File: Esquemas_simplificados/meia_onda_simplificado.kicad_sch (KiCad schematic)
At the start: 18 parts

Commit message: update cap 4 - rectificadores
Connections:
- net V_{G}+ is gone; now on net V_{G}-: K_{1b}.1 (A)
- net V_{G}-: no longer K_{1a}.1 (A)
- new net V_{G+}: K_{1a}.1 (A)
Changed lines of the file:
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@@
 		(end 111.76 41.91)
 		(stroke
-			(width 0)
-			(type default)
+			(width 0.3)
+			(type dash)
+			(color 255 0 0 1)
 		)
 		(fill
@@
 		(end 74.93 59.69)
 		(stroke
-			(width 0)
-			(type default)
+			(width 0.3)
+			(type dash)
+			(color 0 0 132 1)
 		)
 		(fill
@@
 		)
 	)
-	(label "V_{G}-"
+	(label "V_{G+}"
 		(at 58.42 45.72 180)
 		(fields_autoplaced yes)
@@
 		)
 	)
-	(label "V_{G}+"
+	(label "V_{G}-"
 		(at 58.42 48.26 180)
 		(fields_autoplaced yes)
@@
 		(dnp no)
 		(property "Reference" "K_{7a}"
-			(at 122.936 34.544 0)
+			(at 124.46 36.068 0)
 			(effects
 				(font
@@
 		(dnp no)
 		(property "Reference" "K_{1a}"
-			(at 68.58 35.306 0)
+			(at 68.072 36.576 0)
 			(effects
 				(font
@@
 		)
 		(instances
-			(project ""
+			(project "meia_onda_simplificado"
 				(path "/503ffb7c-03f1-4b74-8c9a-f81a98559f55"
 					(reference "K_{1a}")
@@
 		)
 		(instances
-			(project ""
+			(project "meia_onda_simplificado"
 				(path "/503ffb7c-03f1-4b74-8c9a-f81a98559f55"
 					(reference "R2")
@@
 		(dnp no)
 		(property "Reference" "K_{1b}"
-			(at 69.342 50.8 0)
+			(at 67.818 51.816 0)
 			(effects
 				(font
@@
 		)
 		(instances
-			(project ""
+			(project "meia_onda_simplificado"
 				(path "/503ffb7c-03f1-4b74-8c9a-f81a98559f55"
 					(reference "K_{1b}")
@@
 		(dnp no)
 		(property "Reference" "K_{7b}"
-			(at 122.936 59.944 0)
+			(at 124.968 61.468 0)
 			(effects
 				(font
@@
 		(dnp no)
 		(property "Reference" "K_{6a}"
-			(at 114.046 34.544 0)
+			(at 115.57 36.068 0)
 			(effects
 				(font
@@
 		(dnp no)
 		(property "Reference" "K_{3a}"
-			(at 82.55 35.306 0)
+			(at 81.534 36.576 0)
 			(effects
 				(font
@@
 		)
 		(instances
-			(project ""
+			(project "meia_onda_simplificado"
 				(path "/503ffb7c-03f1-4b74-8c9a-f81a98559f55"
 					(reference "K_{3a}")
@@
 		(dnp no)
 		(property "Reference" "K_{9b}"
-			(at 140.716 59.944 0)
+			(at 142.494 61.468 0)
 			(effects
 				(font
@@
 		(dnp no)
 		(property "Reference" "K_{6b}"
-			(at 114.046 59.944 0)
+			(at 116.078 61.468 0)
 			(effects
 				(font
@@
 		)
 		(instances
-			(project ""
+			(project "meia_onda_simplificado"
 				(path "/503ffb7c-03f1-4b74-8c9a-f81a98559f55"
 					(reference "D1")
@@
 		(dnp no)
 		(property "Reference" "K_{3b}"
-			(at 105.156 35.306 0)
+			(at 104.14 36.83 0)
 			(effects
 				(font
@@
 		)
 		(instances
-			(project ""
+			(project "meia_onda_simplificado"
 				(path "/503ffb7c-03f1-4b74-8c9a-f81a98559f55"
 					(reference "K_{3b}")
@@
 		)
 		(instances
-			(project ""
+			(project "meia_onda_simplificado"
 				(path "/503ffb7c-03f1-4b74-8c9a-f81a98559f55"
 					(reference "R1")
@@
 		)
 		(instances
-			(project ""
+			(project "meia_onda_simplificado"
 				(path "/503ffb7c-03f1-4b74-8c9a-f81a98559f55"
 					(reference "C2")
@@
 		(dnp no)
 		(property "Reference" "K_{8a}"
-			(at 131.826 34.544 0)
+			(at 133.35 36.068 0)
 			(effects
 				(font
@@
 		(dnp no)
 		(property "Reference" "K_{9a}"
-			(at 140.716 34.544 0)
+			(at 142.748 36.068 0)
 			(effects
 				(font
@@
 		)
 		(instances
-			(project ""
+			(project "meia_onda_simplificado"
 				(path "/503ffb7c-03f1-4b74-8c9a-f81a98559f55"
 					(reference "C1")
@@
 		(dnp no)
 		(property "Reference" "K_{4}"
-			(at 93.98 51.308 0)
+			(at 92.964 52.324 0)
 			(effects
 				(font
@@
 		)
 		(instances
-			(project ""
+			(project "meia_onda_simplificado"
 				(path "/503ffb7c-03f1-4b74-8c9a-f81a98559f55"
 					(reference "K_{4}")
@@
 		(dnp no)
 		(property "Reference" "K_{8b}"
-			(at 131.826 59.944 0)
-			(effects
-				(font
+			(at 133.604 61.468 0)
+			(effects
+				(font

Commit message: update rectificação cap 4
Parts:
- added D2: B250C2300-1500A, Diode_THT:Diode_Bridge_19.0x3.5x10.0mm_P5.0mm, symbol Diode_Bridge:B250C2300-1500A
- added K_{2a}, K_{2b}, K_{5a}, K_{5b}: SW_SPST, symbol Switch:SW_SPST
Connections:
- net A: now reaches K_{3b}.2 (B), K_{6a}.2 (B), K_{7a}.2 (B), K_{8a}.2 (B), K_{9a}.2 (B)
- net A: now also K_{5a}.2 (B)
- net B: now reaches K_{4}.2 (B), K_{6b}.1 (A), K_{7b}.1 (A), K_{8b}.1 (A), K_{9b}.1 (A)
- net B: now also K_{5b}.2 (B)
- net V_{G}- renamed V_{G-}
- new net: D2.4 (+), K_{5a}.1 (A)
- new net: D2.2, K_{2a}.2 (B)
- new net: D2.3, K_{2b}.2 (B)
- new net: D2.1 (-), K_{5b}.1 (A)
- new net transf+: K_{2a}.1 (A)
- new net transf-: K_{2b}.1 (A)
- no-connect marks 0 -> 4
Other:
- note added: "Filtragem (Comum)"
- note added: "Meia Onda"
- note added: "Onda Completa"
- moved on the sheet: C1, C2, D1, K_{1a}, K_{1b}, K_{3a}, K_{3b}, K_{4}, K_{6a}, K_{6b}, K_{7a}, K_{7b}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

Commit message: update chap 4 - filtros
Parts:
- added C3: 10uF, Capacitor_THT:CP_Radial_D5.0mm_P2.00mm, symbol Device:C_Polarized
- added K_{10}, K_{11}: SW_SPST, symbol Switch:SW_SPST
- added R3: 1K, Resistor_THT:R_Axial_DIN0207_L6.3mm_D2.5mm_P15.24mm_Horizontal, symbol Device:R
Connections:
- net A: now also C3.2, R3.1
- net V_{G+} renamed v_{g+}
- net v_{g+}: now also K_{10}.1 (A), K_{11}.1 (A)
- net V_{G-} renamed v_{g-}
- new net: K_{10}.2 (B), R3.2
- new net: C3.1, K_{11}.2 (B)
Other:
- note removed: "Filtragem (Comum)"
- note removed: "Meia Onda"
- moved on the sheet: C1, C2, D1, D2, K_{1a}, K_{1b}, K_{2a}, K_{2b}, K_{3a}, K_{3b}, K_{4}, K_{5a}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

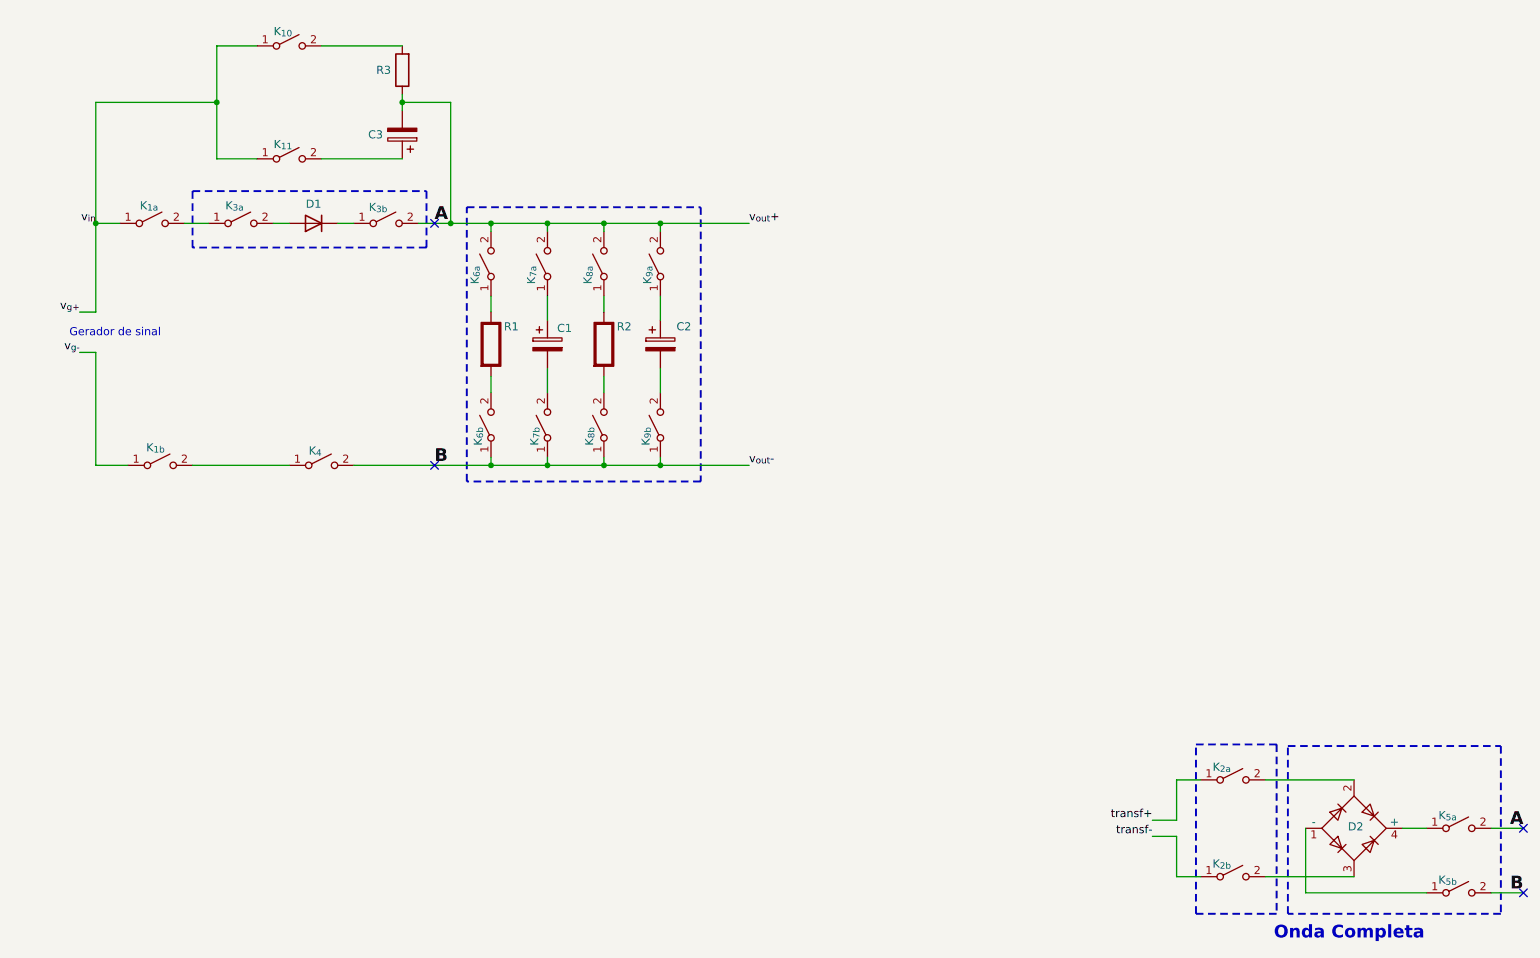
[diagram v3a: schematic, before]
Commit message: update chap 4 - modificação do texto dos filtros e rectificadores
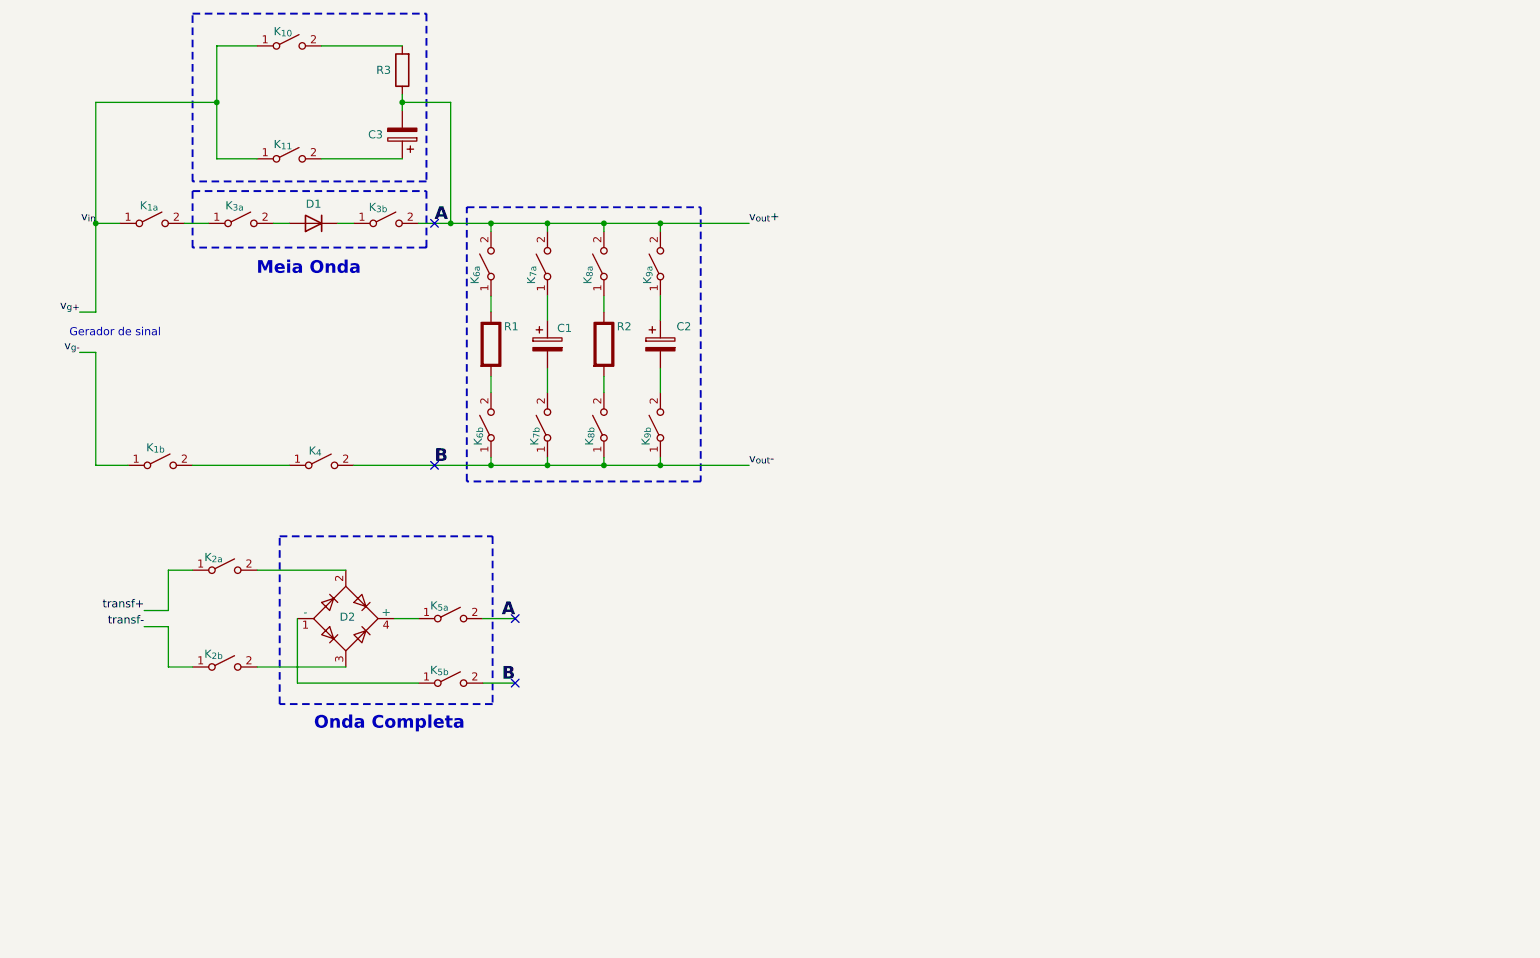
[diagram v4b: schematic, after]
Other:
- note added: "Meia Onda"
- moved on the sheet: D2, K_{2a}, K_{2b}, K_{5a}, K_{5b}
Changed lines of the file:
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@@
 	)
 	(no_connect
-		(at 251.46 142.24)
+		(at 92.71 109.22)
 	)
 	(no_connect
@@
 	)
 	(no_connect
-		(at 251.46 152.4)
+		(at 92.71 119.38)
 	)
 	(wire
@@
 	(wire
 		(pts
-			(xy 210.82 134.62) (xy 224.79 134.62)
-		)
-		(stroke
-			(width 0)
-			(type default)
-		)
-	)
-	(wire
-		(pts
-			(xy 236.22 142.24) (xy 232.41 142.24)
-		)
-		(stroke
-			(width 0)
-			(type default)
-		)
-	)
-	(wire
-		(pts
-			(xy 196.85 143.51) (xy 196.85 149.86)
+			(xy 52.07 101.6) (xy 66.04 101.6)
+		)
+		(stroke
+			(width 0)
+			(type default)
+		)
+	)
+	(wire
+		(pts
+			(xy 77.47 109.22) (xy 73.66 109.22)
+		)
+		(stroke
+			(width 0)
+			(type default)
+		)
+	)
+	(wire
+		(pts
+			(xy 38.1 110.49) (xy 38.1 116.84)
 		)
 		(stroke
@@
 	(wire
 		(pts
-			(xy 196.85 134.62) (xy 196.85 140.97)
+			(xy 38.1 101.6) (xy 38.1 107.95)
 		)
 		(stroke
@@
 	(wire
 		(pts
-			(xy 210.82 149.86) (xy 224.79 149.86)
+			(xy 52.07 116.84) (xy 66.04 116.84)
 		)
 		(stroke
@@
 	(wire
 		(pts
-			(xy 217.17 142.24) (xy 217.17 152.4)
+			(xy 58.42 109.22) (xy 58.42 119.38)
 		)
 		(stroke
@@
 	(wire
 		(pts
-			(xy 196.85 149.86) (xy 200.66 149.86)
+			(xy 38.1 116.84) (xy 41.91 116.84)
 		)
 		(stroke
@@
 	(wire
 		(pts
-			(xy 246.38 142.24) (xy 251.46 142.24)
+			(xy 87.63 109.22) (xy 92.71 109.22)
 		)
 		(stroke
@@
 	(wire
 		(pts
-			(xy 217.17 152.4) (xy 236.22 152.4)
+			(xy 58.42 119.38) (xy 77.47 119.38)
 		)
 		(stroke
@@
 	(wire
 		(pts
-			(xy 193.04 143.51) (xy 196.85 143.51)
+			(xy 34.29 110.49) (xy 38.1 110.49)
 		)
 		(stroke
@@
 	(wire
 		(pts
-			(xy 196.85 134.62) (xy 200.66 134.62)
-		)
-		(stroke
-			(width 0)
-			(type default)
-		)
-	)
-	(wire
-		(pts
-			(xy 246.38 152.4) (xy 251.46 152.4)
+			(xy 38.1 101.6) (xy 41.91 101.6)
+		)
+		(stroke
+			(width 0)
+			(type default)
+		)
+	)
+	(wire
+		(pts
+			(xy 87.63 119.38) (xy 92.71 119.38)
 		)
 		(stroke
@@
 	(wire
 		(pts
-			(xy 193.04 140.97) (xy 196.85 140.97)
+			(xy 34.29 107.95) (xy 38.1 107.95)
 		)
 		(stroke
@@
 	)
 	(rectangle
-		(start 199.898 129.032)
-		(end 212.598 155.702)
+		(start 55.626 96.266)
+		(end 89.154 122.682)
 		(stroke
 			(width 0.3)
 			(type dash)
-			(color 78 222 255 1)
+			(color 0 132 0 1)
 		)
 		(fill
@@
 	)
 	(rectangle
-		(start 214.376 129.286)
-		(end 247.904 155.702)
+		(start 41.91 13.97)
+		(end 78.74 40.386)
 		(stroke
 			(width 0.3)
 			(type dash)
-			(color 255 115 114 1)
+			(color 255 0 255 1)
 		)
 		(fill
@@
 	(text "Onda Completa"
 		(exclude_from_sim no)
-		(at 224.028 158.75 0)
+		(at 72.898 125.73 0)
 		(effects
 			(font
@@
 		)
 	)
+	(text "Meia Onda"
+		(exclude_from_sim no)
+		(at 60.198 54.102 0)
+		(effects
+			(font
+				(size 2 2)
+				(bold yes)
+			)
+		)
+	)
 	(label "B"
-		(at 251.46 152.4 180)
+		(at 92.71 119.38 180)
 		(fields_autoplaced yes)
 		(effects
@@
 	)
 	(label "transf-"
-		(at 193.04 143.51 180)
+		(at 34.29 110.49 180)
 		(fields_autoplaced yes)
 		(effects
@@
 	)
 	(label "transf+"
-		(at 193.04 140.97 180)
+		(at 34.29 107.95 180)
 		(fields_autoplaced yes)
 		(effects
@@
 	)
 	(label "A"
-		(at 251.46 142.24 180)
+		(at 92.71 109.22 180)
 		(fields_autoplaced yes)
 		(effects
@@
 	(symbol
 		(lib_id "Switch:SW_SPST")
-		(at 241.3 142.24 0)
+		(at 82.55 109.22 0)
 		(unit 1)
 		(exclude_from_sim no)
@@
 		(dnp no)
 		(property "Reference" "K_{5a}"
-			(at 239.522 140.208 0)
+			(at 80.772 107.188 0)
 			(effects
 				(font
@@
 		)
 		(property "Value" "SW_SPST"
-			(at 241.3 138.43 0)
+			(at 82.55 105.41 0)
 			(effects
 				(font
@@
 		)
 		(property "Footprint" ""
-			(at 241.3 142.24 0)
+			(at 82.55 109.22 0)
 			(effects
 				(font
@@
 		)
 		(property "Datasheet" "~"
-			(at 241.3 142.24 0)
+			(at 82.55 109.22 0)
 			(effects
 				(font
@@
 		)
 		(property "Description" "Single Pole Single Throw (SPST) switch"
-			(at 241.3 142.24 0)
+			(at 82.55 109.22 0)
 			(effects
 				(font
@@
 	(symbol
 		(lib_id "Switch:SW_SPST")
-		(at 205.74 134.62 0)
+		(at 46.99 101.6 0)
 		(unit 1)
 		(exclude_from_sim no)
@@
 		(dnp no)
 		(property "Reference" "K_{2a}"
-			(at 203.962 132.588 0)
+			(at 45.212 99.568 0)
 			(effects
 				(font
@@
 		)
 		(property "Value" "SW_SPST"
-			(at 205.74 130.81 0)
+			(at 46.99 97.79 0)
 			(effects
 				(font
@@
 		)
 		(property "Footprint" ""
-			(at 205.74 134.62 0)
+			(at 46.99 101.6 0)
 			(effects
 				(font
@@
 		)
 		(property "Datasheet" "~"
-			(at 205.74 134.62 0)
+			(at 46.99 101.6 0)
 			(effects
 				(font
@@
 		)
 		(property "Description" "Single Pole Single Throw (SPST) switch"
-			(at 205.74 134.62 0)
+			(at 46.99 101.6 0)
 			(effects
 				(font
@@
 	(symbol
 		(lib_id "Switch:SW_SPST")
-		(at 205.74 149.86 0)
+		(at 46.99 116.84 0)
 		(unit 1)
 		(exclude_from_sim no)
@@
 		(dnp no)
 		(property "Reference" "K_{2b}"
-			(at 203.962 147.828 0)
+			(at 45.212 114.808 0)
 			(effects
 				(font
@@
 		)
 		(property "Value" "SW_SPST"
-			(at 205.74 146.05 0)
+			(at 46.99 113.03 0)
 			(effects
 				(font
@@
 		)
 		(property "Footprint" ""
-			(at 205.74 149.86 0)
+			(at 46.99 116.84 0)
 			(effects
 				(font
@@
 		)
 		(property "Datasheet" "~"
-			(at 205.74 149.86 0)
+			(at 46.99 116.84 0)
 			(effects
 				(font
@@
 		)
 		(property "Description" "Single Pole Single Throw (SPST) switch"
-			(at 205.74 149.86 0)
+			(at 46.99 116.84 0)
 			(effects
 				(font
@@
 	(symbol
 		(lib_id "Switch:SW_SPST")
-		(at 241.3 152.4 0)
+		(at 82.55 119.38 0)
 		(unit 1)
 		(exclude_from_sim no)
@@
 		(dnp no)
 		(property "Reference" "K_{5b}"
-			(at 239.522 150.368 0)
+			(at 80.772 117.348 0)
 			(effects
 				(font
@@
 		)
 		(property "Value" "SW_SPST"
-			(at 241.3 148.59 0)
+			(at 82.55 115.57 0)
 			(effects
 				(font
@@
 		)
 		(property "Footprint" ""
-			(at 241.3 152.4 0)
+			(at 82.55 119.38 0)
 			(effects
 				(font
@@
 		)
 		(property "Datasheet" "~"
-			(at 241.3 152.4 0)
+			(at 82.55 119.38 0)
 			(effects
 				(font
@@
 		)
 		(property "Description" "Single Pole Single Throw (SPST) switch"
-			(at 241.3 152.4 0)
+			(at 82.55 119.38 0)
 			(effects
 				(font
@@
 	(symbol
 		(lib_id "Diode_Bridge:B250C2300-1500A")
-		(at 224.79 142.24 0)
+		(at 66.04 109.22 0)
 		(unit 1)
 		(exclude_from_sim no)
@@
 		(dnp no)
 		(property "Reference" "D2"
-			(at 225.044 141.986 0)
+			(at 66.294 108.966 0)
 			(effects
 				(font
@@
 		)
 		(property "Value" "B250C2300-1500A"
-			(at 226.568 160.274 0)
+			(at 67.818 127.254 0)
 			(effects
 				(font
@@
 		)
 		(property "Footprint" "Diode_THT:Diode_Bridge_19.0x3.5x10.0mm_P5.0mm"
-			(at 228.6 139.065 0)
+			(at 69.85 106.045 0)
 			(effects
 				(font
@@
 		)
 		(property "Datasheet" "https://diotec.com/tl_files/diotec/files/pdf/datasheets/b40c2300.pdf"
-			(at 224.79 142.24 0)
+			(at 66.04 109.22 0)
 			(effects
 				(font
@@
 		)
 		(property "Description" "Silicon Bridge Rectifier, 250V Vrms, 1.5A If, pins=-AA+, SIL-package"
-			(at 224.79 142.24 0)
-			(effects
-				(font
+			(at 66.04 109.22 0)
+			(effects
+				(font
